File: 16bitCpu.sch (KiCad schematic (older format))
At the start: 0 parts

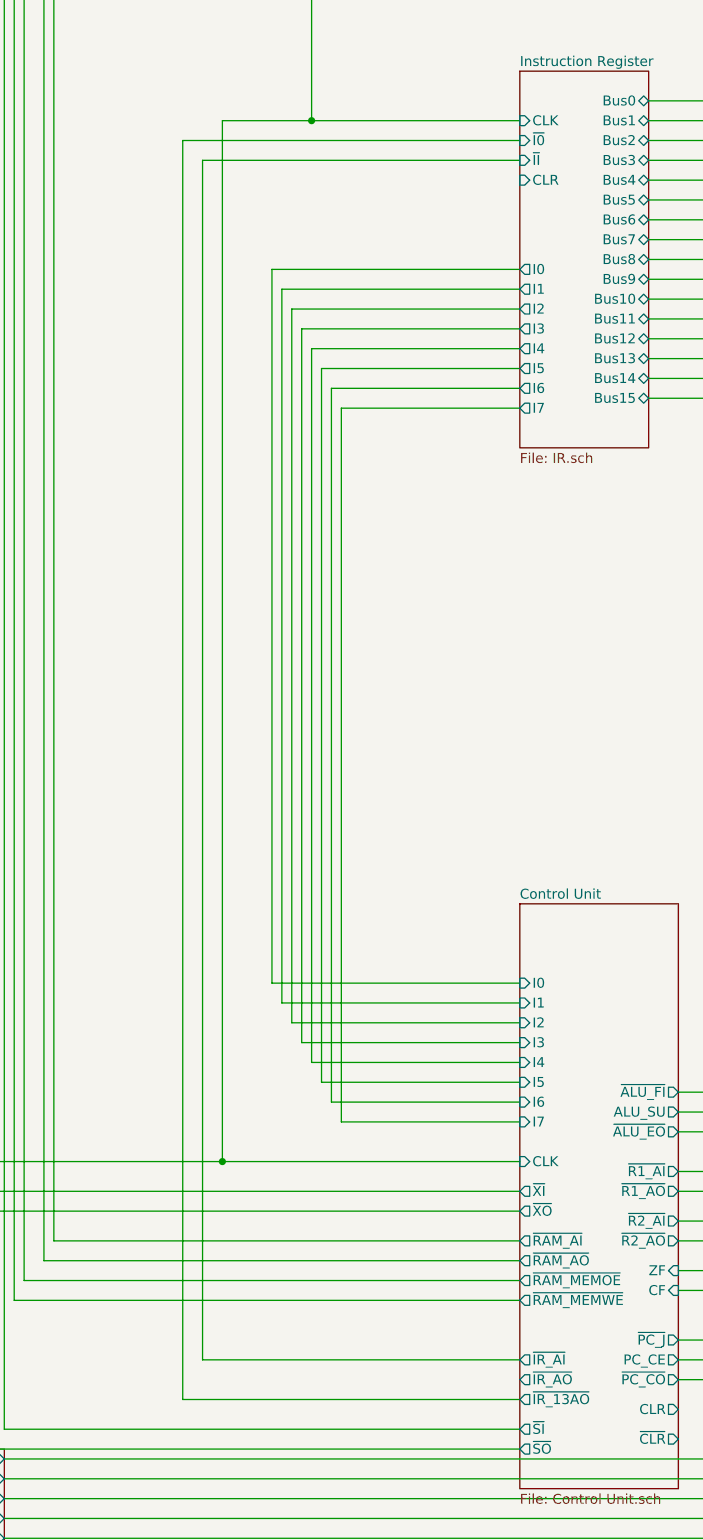
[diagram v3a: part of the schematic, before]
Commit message: back to 13 bit addresses
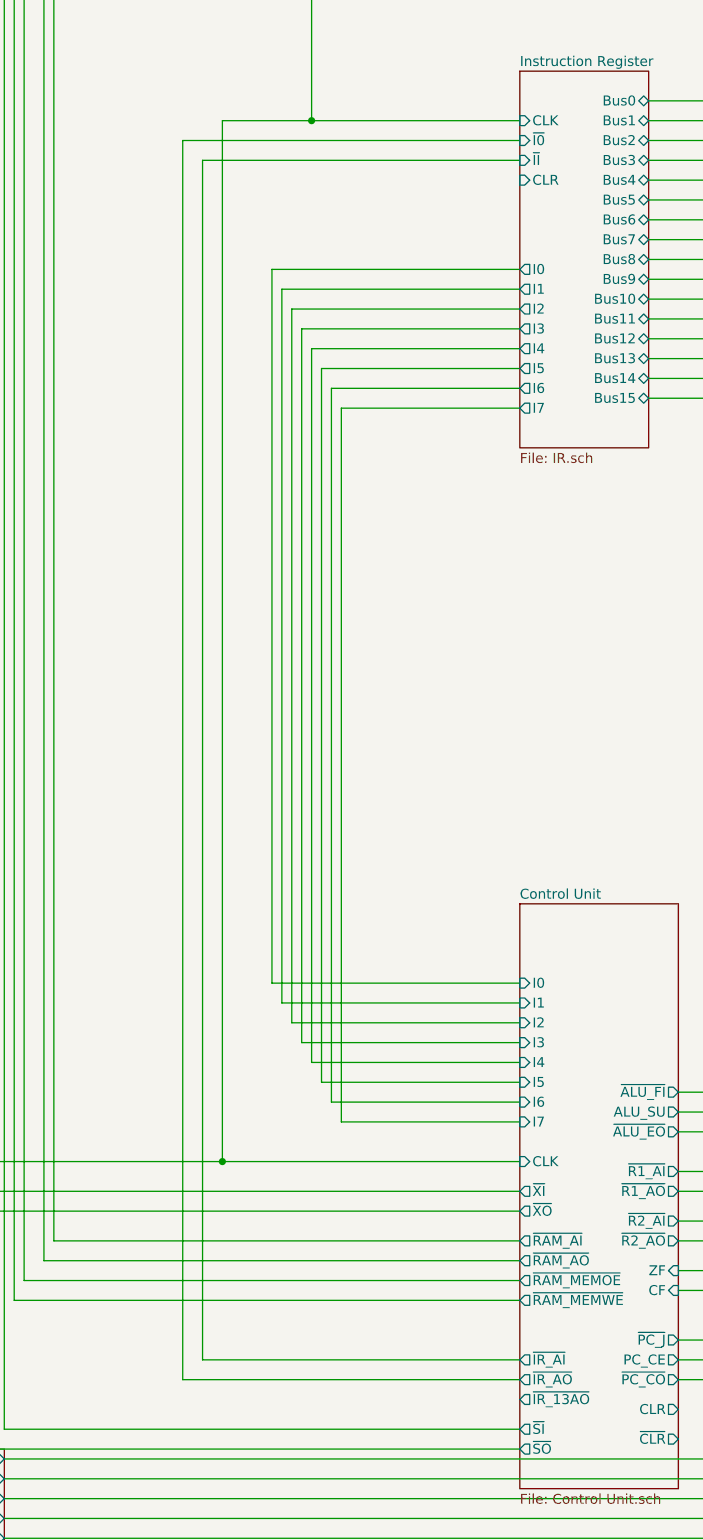
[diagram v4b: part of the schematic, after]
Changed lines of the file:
@@
 	2650 7450 4350 7450
-Wire Wire Line
-	4350 13800 2650 13800
-Wire Wire Line
-	2650 7450 2650 13800
 Wire Wire Line
 	7400 550  7400 2100
@@
 	600  14150 950  14150
 Connection ~ 2850 12600
+Wire Wire Line
+	4350 13700 2650 13700
+Wire Wire Line
+	2650 7450 2650 13700
 $EndSCHEMATC

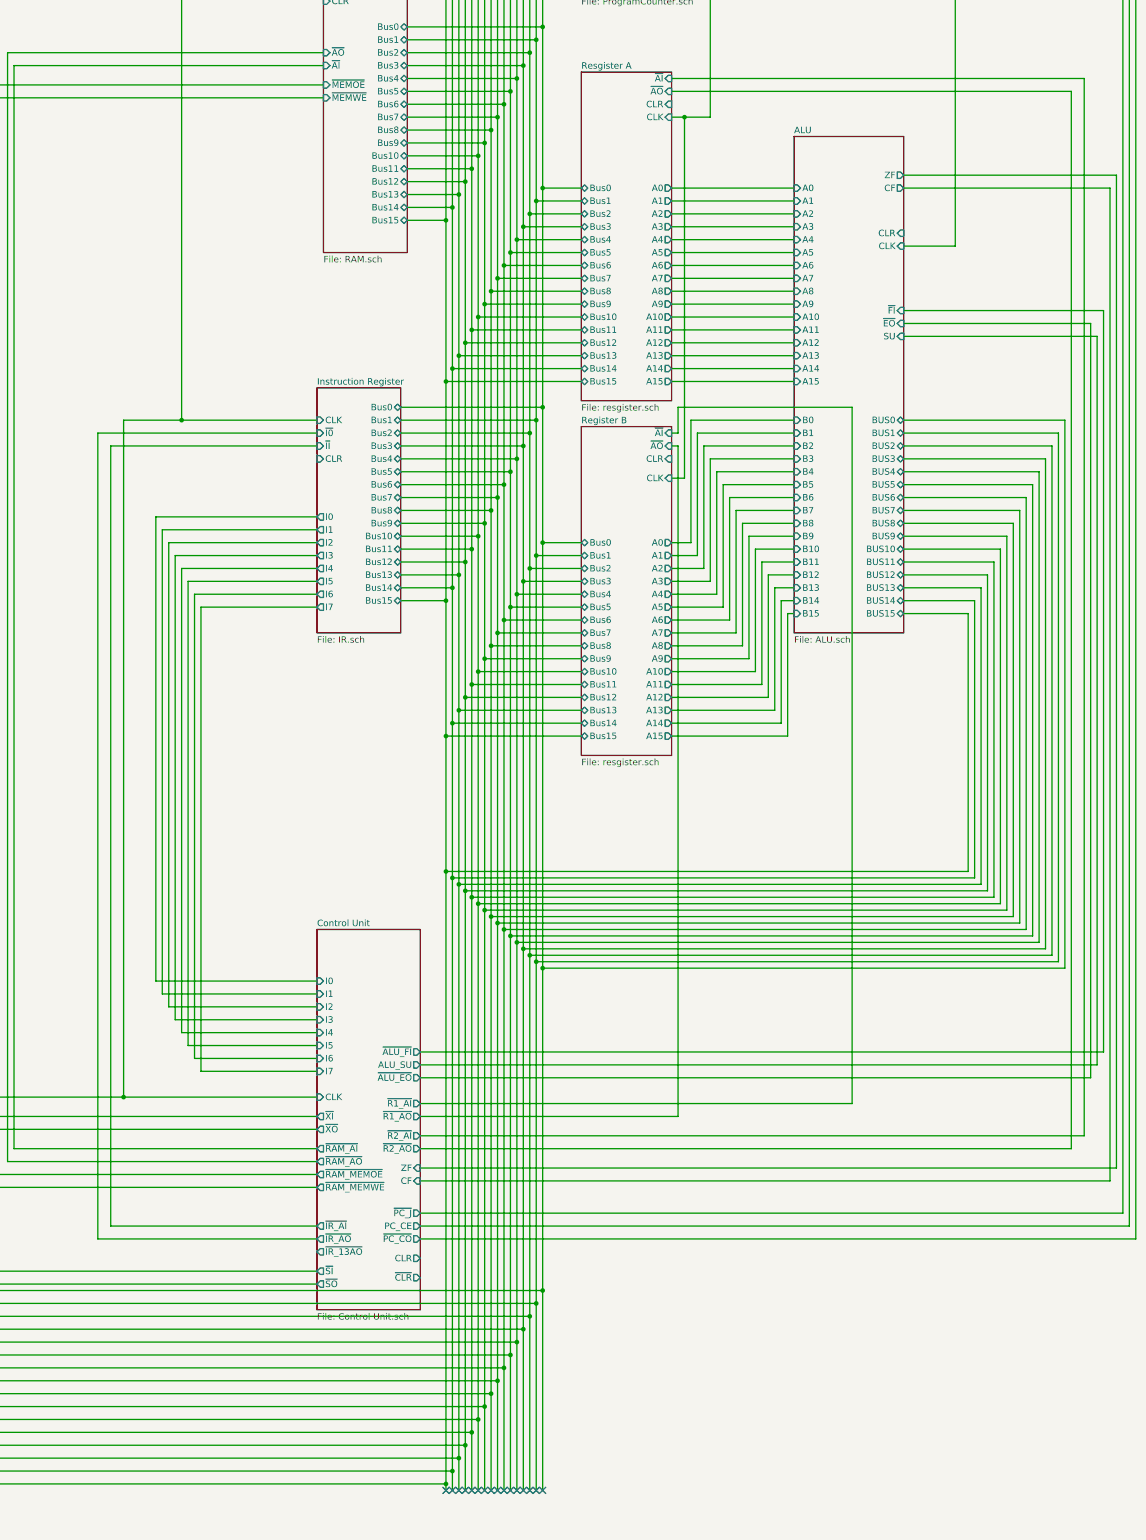
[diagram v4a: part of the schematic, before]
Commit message: Added 8 bit output to the ir
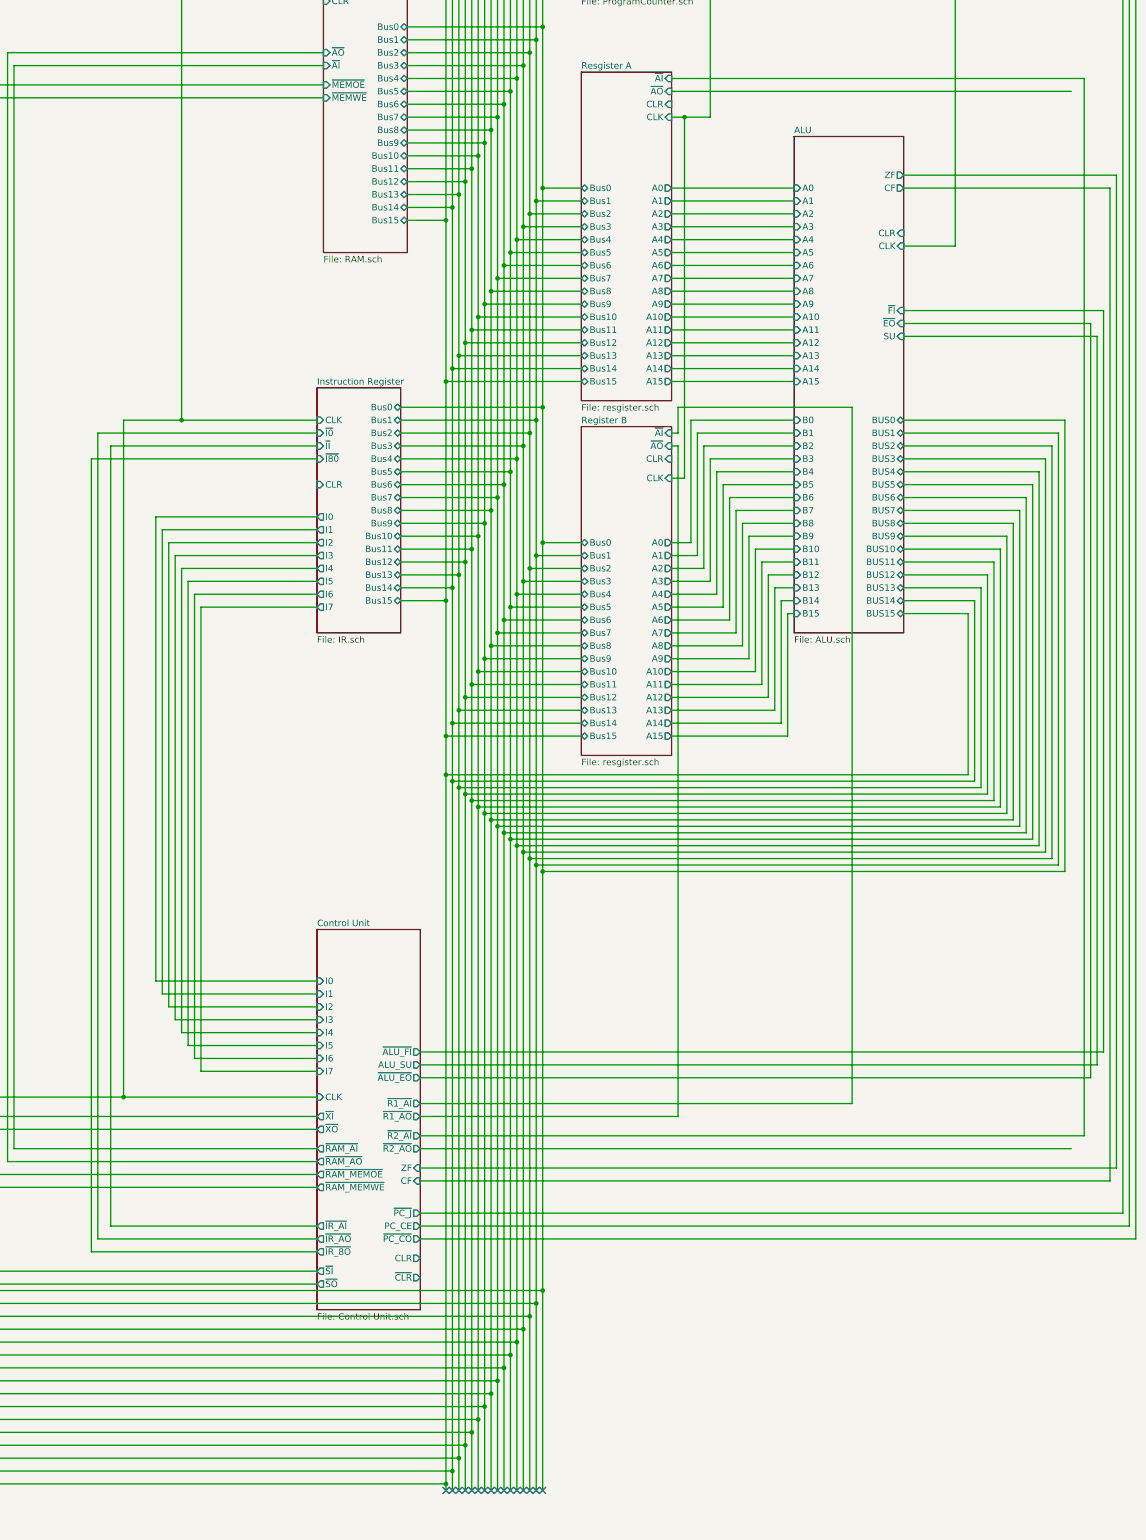
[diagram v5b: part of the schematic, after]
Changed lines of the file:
@@
 Wire Wire Line
 	7100 5550 8050 5550
-Wire Wire Line
-	9400 8850 9400 10850
-Wire Wire Line
-	5350 10850 9400 10850
-Wire Wire Line
-	9450 8750 9450 10900
-Wire Wire Line
-	5400 10900 9450 10900
-Wire Wire Line
-	5450 10950 9500 10950
-Wire Wire Line
-	9500 8650 9500 10950
-Wire Wire Line
-	9550 8550 9550 11000
-Wire Wire Line
-	5500 11000 9550 11000
-Wire Wire Line
-	5550 11050 9600 11050
-Wire Wire Line
-	9600 8450 9600 11050
-Wire Wire Line
-	9650 8350 9650 11100
-Wire Wire Line
-	5600 11100 9650 11100
-Wire Wire Line
-	5650 11150 9700 11150
-Wire Wire Line
-	9700 8250 9700 11150
-Wire Wire Line
-	9750 8150 9750 11200
-Wire Wire Line
-	5700 11200 9750 11200
-Wire Wire Line
-	9800 8050 9800 11250
-Wire Wire Line
-	5750 11250 9800 11250
-Wire Wire Line
-	5800 11300 9850 11300
-Wire Wire Line
-	9850 7950 9850 11300
-Wire Wire Line
-	9900 7850 9900 11350
-Wire Wire Line
-	5850 11350 9900 11350
-Wire Wire Line
-	9950 7750 9950 11400
-Wire Wire Line
-	5900 11400 9950 11400
-Wire Wire Line
-	10000 7650 10000 11450
-Wire Wire Line
-	5950 11450 10000 11450
-Wire Wire Line
-	6000 11500 10050 11500
-Wire Wire Line
-	10050 7550 10050 11500
-Wire Wire Line
-	6050 11550 10100 11550
-Wire Wire Line
-	10100 7450 10100 11550
-Wire Wire Line
-	10150 7350 10150 11600
-Wire Wire Line
-	6100 11600 10150 11600
 $Sheet
 S 6400 7400 700  2550
@@
 Connection ~ 5350 7050
 Connection ~ 5350 9800
-Wire Wire Line
-	5350 9800 5350 10850
-Connection ~ 5350 10850
 Connection ~ 5400 6950
 Connection ~ 5400 9700
-Connection ~ 5400 10900
 Connection ~ 5450 6850
 Connection ~ 5450 9600
-Connection ~ 5450 10950
 Connection ~ 5500 6750
 Connection ~ 5500 9500
-Connection ~ 5500 11000
 Connection ~ 5550 6650
 Connection ~ 5550 9400
-Connection ~ 5550 11050
 Connection ~ 5600 6550
 Connection ~ 5600 9300
-Connection ~ 5600 11100
 Connection ~ 5650 6450
 Connection ~ 5650 9200
-Connection ~ 5650 11150
 Connection ~ 5700 6350
 Connection ~ 5700 9100
-Connection ~ 5700 11200
 Connection ~ 5750 6250
 Connection ~ 5750 9000
-Connection ~ 5750 11250
 Connection ~ 5800 6150
 Connection ~ 5800 8900
-Connection ~ 5800 11300
 Connection ~ 5850 6050
 Connection ~ 5850 8800
-Connection ~ 5850 11350
 Connection ~ 5900 5950
 Connection ~ 5900 8700
-Connection ~ 5900 11400
 Connection ~ 5950 5850
 Connection ~ 5950 8600
-Connection ~ 5950 11450
 Connection ~ 6000 5750
 Connection ~ 6000 8500
-Connection ~ 6000 11500
 Connection ~ 6050 5650
 Connection ~ 6050 8400
-Connection ~ 6050 11550
 Connection ~ 6100 5550
 Connection ~ 6100 8300
-Connection ~ 6100 11600
 Wire Wire Line
 	5350 5800 5350 7050
@@
 	6000 5750 6000 7450
 Wire Wire Line
-	6100 8300 6100 11600
-Wire Wire Line
 	6050 5650 6050 7350
 Wire Wire Line
-	6050 8400 6050 11550
-Wire Wire Line
-	6000 8500 6000 11500
-Wire Wire Line
 	5950 5850 5950 7550
 Wire Wire Line
-	5950 8600 5950 11450
-Wire Wire Line
-	5900 8700 5900 11400
-Wire Wire Line
-	5850 8800 5850 11350
-Wire Wire Line
-	5800 8900 5800 11300
-Wire Wire Line
 	5700 6350 5700 8050
 Wire Wire Line
-	5750 9000 5750 11250
-Wire Wire Line
 	5750 6250 5750 7950
-Wire Wire Line
-	5700 9100 5700 11200
-Wire Wire Line
-	5650 9200 5650 11150
-Wire Wire Line
-	5600 9300 5600 11100
-Wire Wire Line
-	5550 9400 5550 11050
-Wire Wire Line
-	5500 9500 5500 11000
-Wire Wire Line
-	5400 9700 5400 10900
 Wire Wire Line
 	6100 5550 6100 7250
@@
 F3 "Bus0" T R 5000 7250 50
 F4 "~I0" I L 4350 7450 50
-F5 "CLR" I L 4350 7650 50
+F5 "CLR" I L 4350 7850 50
 F6 "Bus1" T R 5000 7350 50
 F7 "Bus2" T R 5000 7450 50
@@
 F28 "I7" O L 4350 8800 50
 F29 "~II" I L 4350 7550 50
+F30 "~I80" I L 4350 7650 50
 $EndSheet
 Wire Wire Line
@@
 Wire Wire Line
 	5350 9800 6400 9800
-Wire Wire Line
-	5450 9600 5450 10950
 Wire Wire Line
 	3100 8100 3100 11700
@@
 F24 "~IR_AI" O L 4350 13600 50
 F25 "~IR_AO" O L 4350 13700 50
-F26 "~IR_13AO" O L 4350 13800 50
-F27 "~PC_J" O R 5150 13500 50
-F28 "PC_CE" O R 5150 13600 50
-F29 "~PC_CO" O R 5150 13700 50
-F30 "CLR" O R 5150 13850 50
-F31 "~CLR" O R 5150 14000 50
-F32 "~SI" O L 4350 13950 50
-F33 "~SO" O L 4350 14050 50
-F34 "~XI" O L 4350 12750 50
-F35 "~XO" O L 4350 12850 50
+F26 "~PC_J" O R 5150 13500 50
+F27 "PC_CE" O R 5150 13600 50
+F28 "~PC_CO" O R 5150 13700 50
+F29 "CLR" O R 5150 13850 50
+F30 "~CLR" O R 5150 14000 50
+F31 "~SI" O L 4350 13950 50
+F32 "~SO" O L 4350 14050 50
+F33 "~XI" O L 4350 12750 50
+F34 "~XO" O L 4350 12850 50
+F35 "~IR_8O" O L 4350 13800 50
 $EndSheet
 Wire Wire Line
-	6050 11550 6050 14200
-Wire Wire Line
-	5950 11450 5950 14400
-Wire Wire Line
-	5850 11350 5850 14600
-Wire Wire Line
-	5750 11250 5750 14800
-Wire Wire Line
-	5700 11200 5700 14900
-Wire Wire Line
-	5600 11100 5600 15100
-Wire Wire Line
-	5550 11050 5550 15200
-Wire Wire Line
-	5500 11000 5500 15300
-Wire Wire Line
 	8900 5450 10550 5450
 Wire Wire Line
@@
 Wire Wire Line
 	5150 13000 10200 13000
-Wire Wire Line
-	10200 13000 10200 4800
 Wire Wire Line
 	10200 4800 7100 4800
@@
 Wire Wire Line
 	1750 15600 5350 15600
-Wire Wire Line
-	5350 10850 5350 15600
 Connection ~ 5350 15600
 Wire Wire Line
@@
 Wire Wire Line
 	1750 15500 5400 15500
-Wire Wire Line
-	5400 10900 5400 15500
 Connection ~ 5400 15500
 Wire Wire Line
@@
 Wire Wire Line
 	1750 15400 5450 15400
-Wire Wire Line
-	5450 10950 5450 15400
 Connection ~ 5450 15400
 Wire Wire Line
@@
 Wire Wire Line
 	1750 15000 5650 15000
-Wire Wire Line
-	5650 11150 5650 15000
 Connection ~ 5650 15000
 Wire Wire Line
@@
 Wire Wire Line
 	1750 14700 5800 14700
-Wire Wire Line
-	5800 11300 5800 14700
 Connection ~ 5800 14700
 Wire Wire Line
@@
 Wire Wire Line
 	1750 14500 5900 14500
-Wire Wire Line
-	5900 11400 5900 14500
 Connection ~ 5900 14500
 Wire Wire Line
@@
 Wire Wire Line
 	1750 14300 6000 14300
-Wire Wire Line
-	6000 11500 6000 14300
 Connection ~ 6000 14300
 Wire Wire Line
@@
 Wire Wire Line
 	1750 14100 6100 14100
-Wire Wire Line
-	6100 11600 6100 14100
 Connection ~ 6100 14100
 Wire Wire Line
@@
 Wire Wire Line
 	2650 7450 2650 13700
+Wire Wire Line
+	4350 7650 2600 7650
+Wire Wire Line
+	2600 7650 2600 13800
+Wire Wire Line
+	2600 13800 4350 13800
+Wire Wire Line
+	10150 7350 10150 10850
+Wire Wire Line
+	10100 7450 10100 10800
+Wire Wire Line
+	10050 7550 10050 10750
+Wire Wire Line
+	10000 7650 10000 10700
+Wire Wire Line
+	9950 7750 9950 10650
+Wire Wire Line
+	9900 7850 9900 10600
+Wire Wire Line
+	9850 7950 9850 10550
+Wire Wire Line
+	9800 8050 9800 10500
+Wire Wire Line
+	9750 8150 9750 10450
+Wire Wire Line
+	9700 8250 9700 10400
+Wire Wire Line
+	9650 8350 9650 10350
+Wire Wire Line
+	9600 8450 9600 10300
+Wire Wire Line
+	9550 8550 9550 10250
+Wire Wire Line
+	9500 8650 9500 10200
+Wire Wire Line
+	9450 8750 9450 10150
+Wire Wire Line
+	9400 8850 9400 10100
+Wire Wire Line
+	6100 8300 6100 10850
+Wire Wire Line
+	6050 8400 6050 10800
+Wire Wire Line
+	6000 8500 6000 10750
+Wire Wire Line
+	5950 8600 5950 10700
+Wire Wire Line
+	5900 8700 5900 10650
+Wire Wire Line
+	5850 8800 5850 10600
+Wire Wire Line
+	5800 8900 5800 10550
+Wire Wire Line
+	5750 9000 5750 10500
+Wire Wire Line
+	5700 9100 5700 10450
+Wire Wire Line
+	5650 9200 5650 10400
+Wire Wire Line
+	5600 9300 5600 10350
+Wire Wire Line
+	5550 9400 5550 10300
+Wire Wire Line
+	5500 9500 5500 10250
+Wire Wire Line
+	5450 9600 5450 10200
+Wire Wire Line
+	5400 9700 5400 10150
+Wire Wire Line
+	5350 9800 5350 10100
+Wire Wire Line
+	5350 10100 9400 10100
+Wire Wire Line
+	5400 10150 9450 10150
+Wire Wire Line
+	5450 10200 9500 10200
+Wire Wire Line
+	5500 10250 9550 10250
+Wire Wire Line
+	5550 10300 9600 10300
+Wire Wire Line
+	5600 10350 9650 10350
+Wire Wire Line
+	5650 10400 9700 10400
+Wire Wire Line
+	5700 10450 9750 10450
+Wire Wire Line
+	5750 10500 9800 10500
+Wire Wire Line
+	5800 10550 9850 10550
+Wire Wire Line
+	5850 10600 9900 10600
+Wire Wire Line
+	5900 10650 9950 10650
+Wire Wire Line
+	5950 10700 10000 10700
+Wire Wire Line
+	6000 10750 10050 10750
+Wire Wire Line
+	6050 10800 10100 10800
+Connection ~ 5350 10100
+Connection ~ 5400 10150
+Connection ~ 5450 10200
+Connection ~ 5500 10250
+Connection ~ 5550 10300
+Connection ~ 5600 10350
+Connection ~ 5650 10400
+Connection ~ 5700 10450
+Connection ~ 5750 10500
+Connection ~ 5800 10550
+Connection ~ 5850 10600
+Connection ~ 5900 10650
+Connection ~ 5950 10700
+Connection ~ 6000 10750
+Connection ~ 6050 10800
+Connection ~ 6100 10850
+Wire Wire Line
+	6050 10800 6050 14200
+Wire Wire Line
+	5950 10700 5950 14400
+Wire Wire Line
+	5850 10600 5850 14600
+Wire Wire Line
+	5750 10500 5750 14800
+Wire Wire Line
+	5700 10450 5700 14900
+Wire Wire Line
+	5600 10350 5600 15100
+Wire Wire Line
+	5550 10300 5550 15200
+Wire Wire Line
+	5500 10250 5500 15300
+Wire Wire Line
+	5350 10100 5350 15600
+Wire Wire Line
+	5400 10150 5400 15500
+Wire Wire Line
+	5450 10200 5450 15400
+Wire Wire Line
+	5650 10400 5650 15000
+Wire Wire Line
+	5800 10550 5800 14700
+Wire Wire Line
+	5900 10650 5900 14500
+Wire Wire Line
+	6000 10750 6000 14300
+Wire Wire Line
+	6100 10850 6100 14100
+Wire Wire Line
+	6100 10850 10150 10850
 $EndSCHEMATC

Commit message: Let there be light
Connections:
- wire segments 495 -> 527
- no-connect marks 31 -> 0

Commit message: Fixes
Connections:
- net labels added: +5V-power, GND-power, VCC-power
- wire segments 527 -> 533
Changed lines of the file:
@@
 F21 "~AI" I L 4400 5150 50
 F22 "~MEMOE" I L 4400 5300 50
-F23 "~MEMWE" I L 4400 5400 50
+F23 "MEMWE" I L 4400 5400 50
 $EndSheet
 $Sheet
@@
 F17 "I15" I B 6950 1050 50
 $EndSheet
+Wire Wire Line
+	9350 1850 9650 1850
+Wire Wire Line
+	9650 1850 9650 1750
+Wire Wire Line
+	9350 2200 9600 2200
+Wire Wire Line
+	9600 2200 9600 2350
+$Comp
+L 16bitCpu-rescue:GND-power #PWR?
+U 1 1 5FAE3C9B
+P 9600 2350
+F 0 "#PWR?" H 9600 2100 50  0001 C CNN
+F 1 "GND-power" H 9605 2177 50  0000 C CNN
+F 2 "" H 9600 2350 50  0001 C CNN
+F 3 "" H 9600 2350 50  0001 C CNN
+	1    9600 2350
+	1    0    0    -1
+$EndComp
+$Comp
+L 16bitCpu-rescue:+5V-power #PWR?
+U 1 1 5FAE3F33
+P 9650 1750
+F 0 "#PWR?" H 9650 1600 50  0001 C CNN
+F 1 "+5V-power" H 9665 1923 50  0000 C CNN
+F 2 "" H 9650 1750 50  0001 C CNN
+F 3 "" H 9650 1750 50  0001 C CNN
+	1    9650 1750
+	1    0    0    -1
+$EndComp
+Wire Wire Line
+	9650 1850 9900 1850
+Wire Wire Line
+	9900 1850 9900 1750
+Connection ~ 9650 1850
+$Comp
+L 16bitCpu-rescue:VCC-power #PWR?
+U 1 1 5FB3A0D7
+P 9900 1750
+F 0 "#PWR?" H 9900 1600 50  0001 C CNN
+F 1 "VCC-power" H 9915 1923 50  0000 C CNN
+F 2 "" H 9900 1750 50  0001 C CNN
+F 3 "" H 9900 1750 50  0001 C CNN
+	1    9900 1750
+	1    0    0    -1
+$EndComp
 $EndSCHEMATC

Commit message: Clean uP
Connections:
- wire segments 533 -> 432
